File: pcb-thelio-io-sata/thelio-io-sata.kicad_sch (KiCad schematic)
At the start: 11 parts

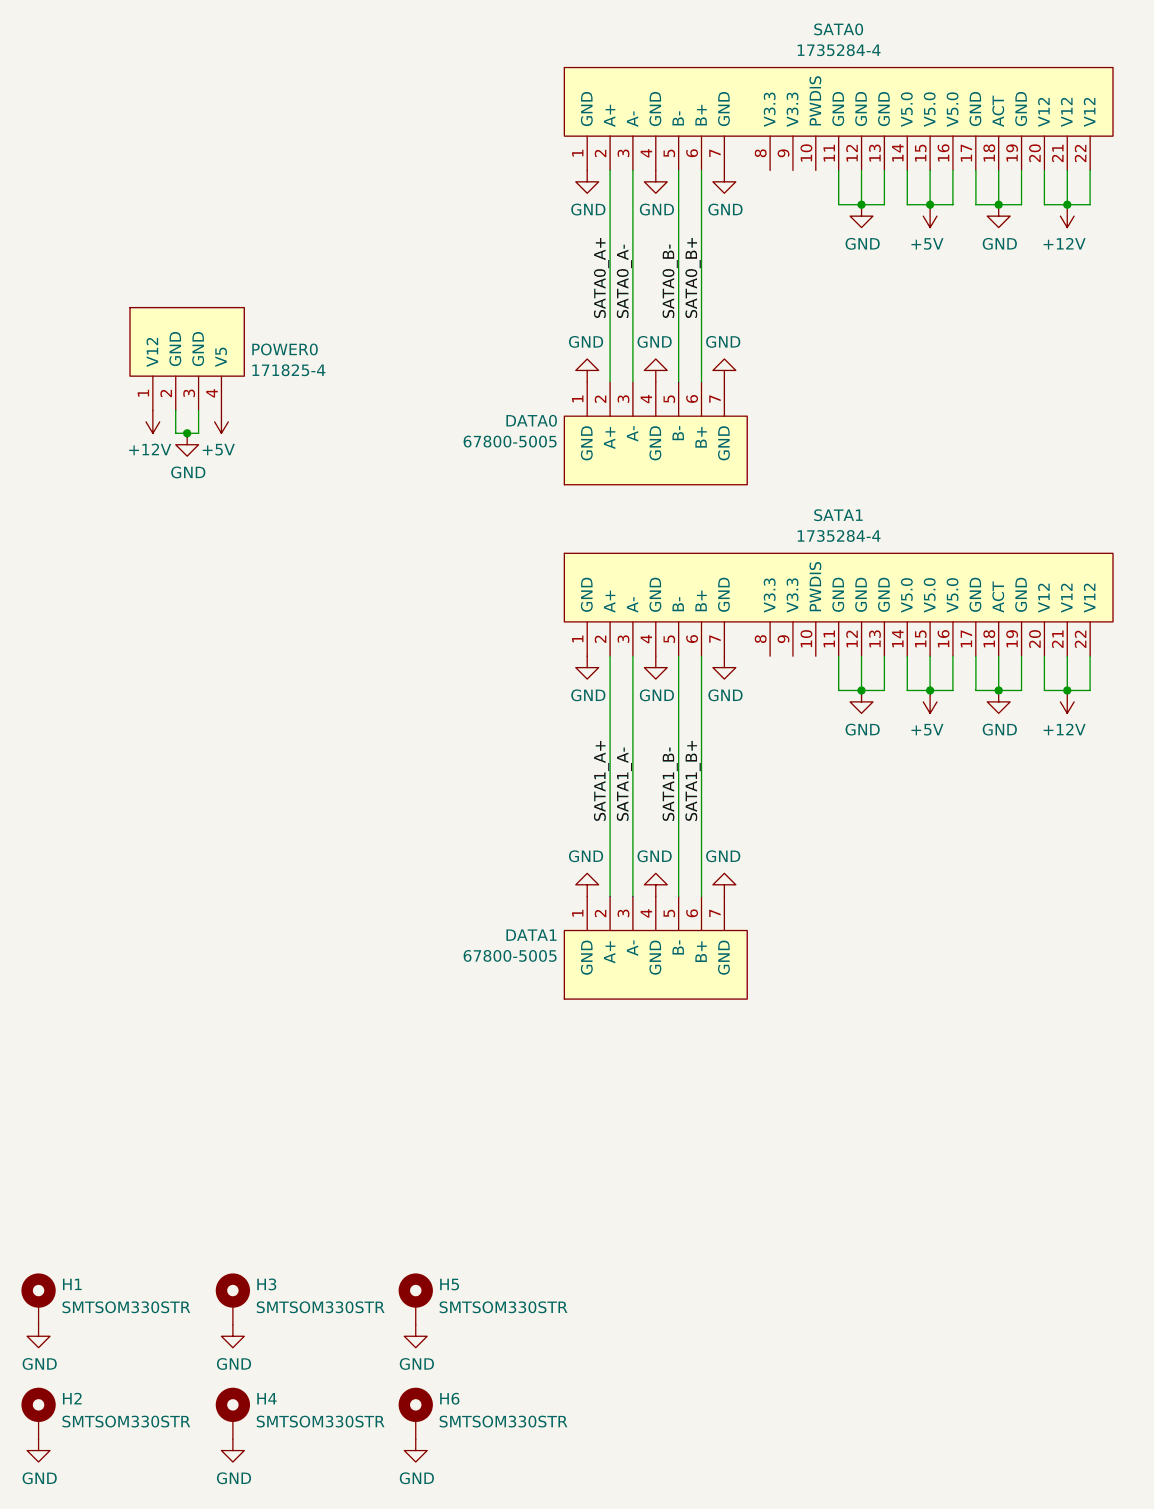
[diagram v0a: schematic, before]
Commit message: thelio-io-sata 2.2 shrink board outline reduce number of mounting standoffs use PEM part number
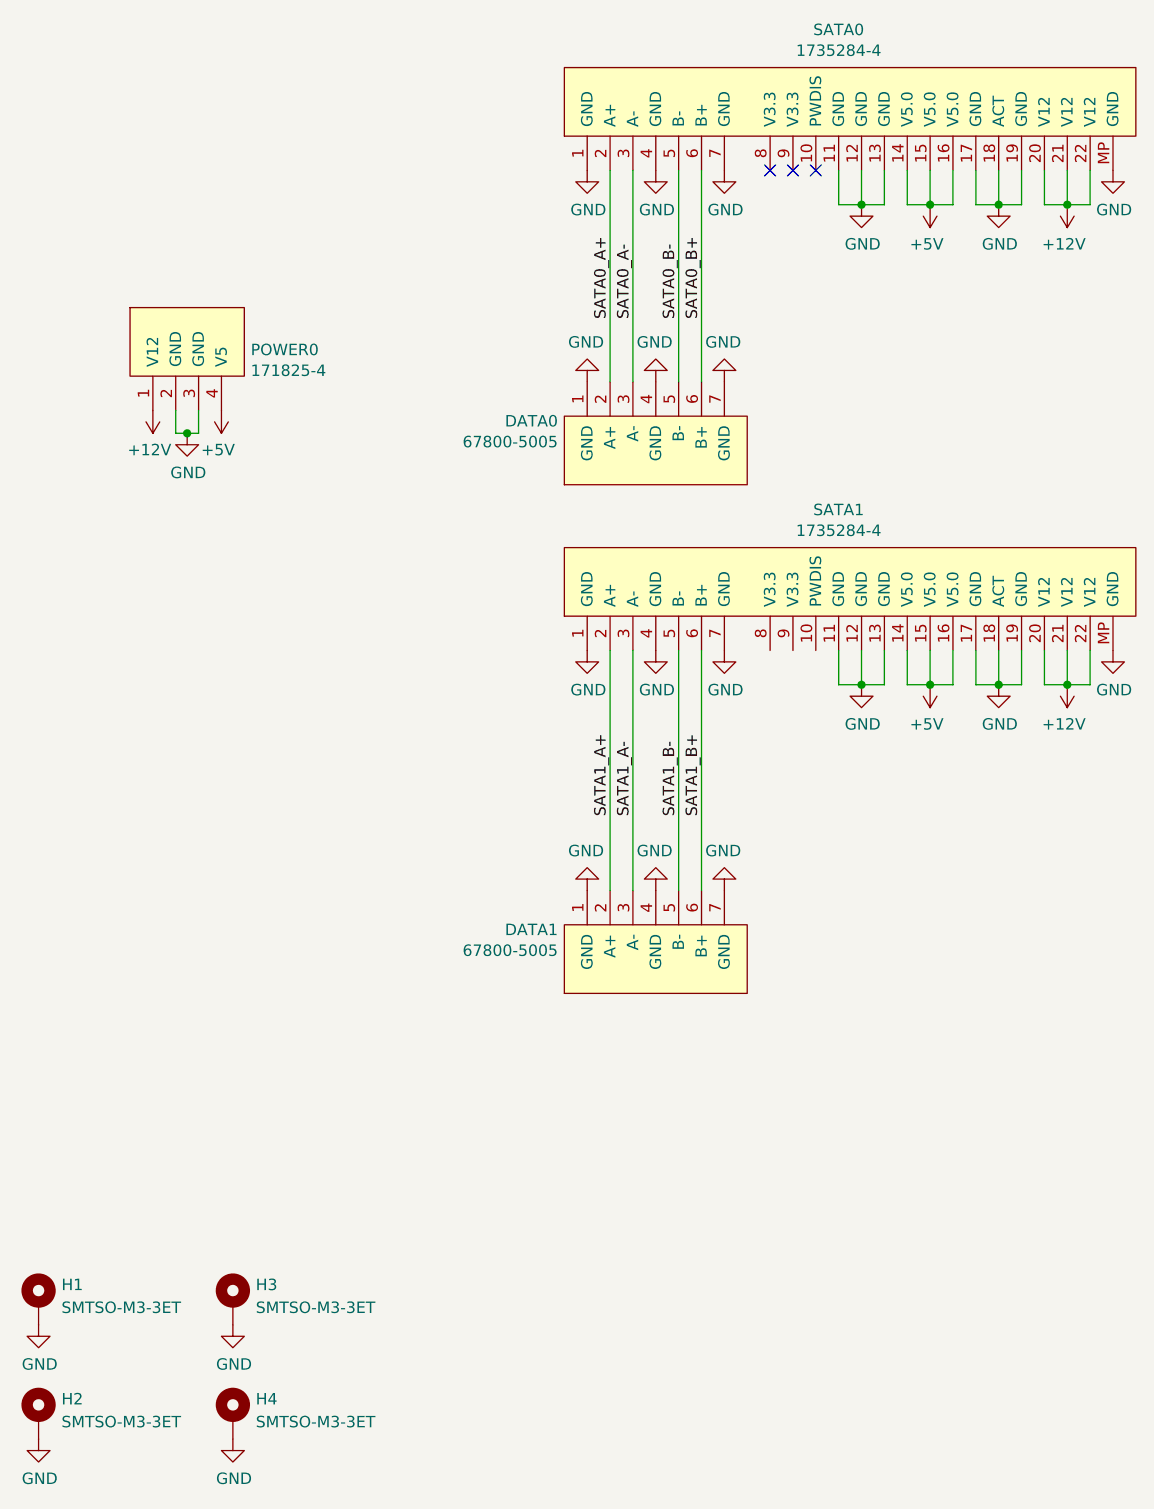
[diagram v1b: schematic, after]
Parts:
- removed H5, H6: SMTSOM330STR, SMTSO:SMTSO-M3-3, symbol Mechanical:MountingHole_Pad
- H1, H2, H3, H4: value SMTSOM330STR -> SMTSO-M3-3ET; Manufacturer Yiyaun -> PEM
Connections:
- net GND: now also SATA0.MP (GND), SATA1.MP (GND)
- no-connect marks 0 -> 3
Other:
- moved on the sheet: DATA1
